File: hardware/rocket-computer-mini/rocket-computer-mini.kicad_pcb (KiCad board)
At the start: 6 copper layers, 222 parts, among them J2 TBLH11-350-05-BK, J3 JST_B2B-PH-SM4-TB, J6 USB4110GFA, J8 CON-SMA-EDGE-S, Q11 AONR21321, Q12 DTC123J, Q3 DTC123J, Q4 DTC123J, Q5 DTC123J, Q6 DTC123J, SW2 R-667995, SW3 R-667995, U1 FSUSB63UMX, U10 WSD20L50DN33, U11 GD5F1GQ5UEYIGR, U13 GD25Q128ESIG, U15 ESP32-S3RH2, U16 E220-900MM22S, U18 TPS62152RGTR, U19 TPS259631DDAR, U2 ISM6HG256XTR, U21 TPS2121RUXR, U23 INA230AIRGTR, U3 QMC5883P, U30 TPS22810DRVR, U31 ANT016008LCS2442MA2, U32 ESP32-S3RH2, U33 GD25Q128ESIG, U4 BMP581, U40 LM66100DCK, U41 74LVC1G17, U42 TPS22810DRVR, U44 LM66100DCK, U45 TPS3840PL29, U5 LC86GLAMD, U6 WSD20L50DN33, U7 WSD20L50DN33, U8 WSD20L50DN33, U9 AON7534, Y1 ABS07-32.768KHZ-T, Y2 ECS-400-10-37B2-CKY-TR, Y3 ABS07-32.768KHZ-T, Y4 ECS-400-10-37B2-CKY-TR

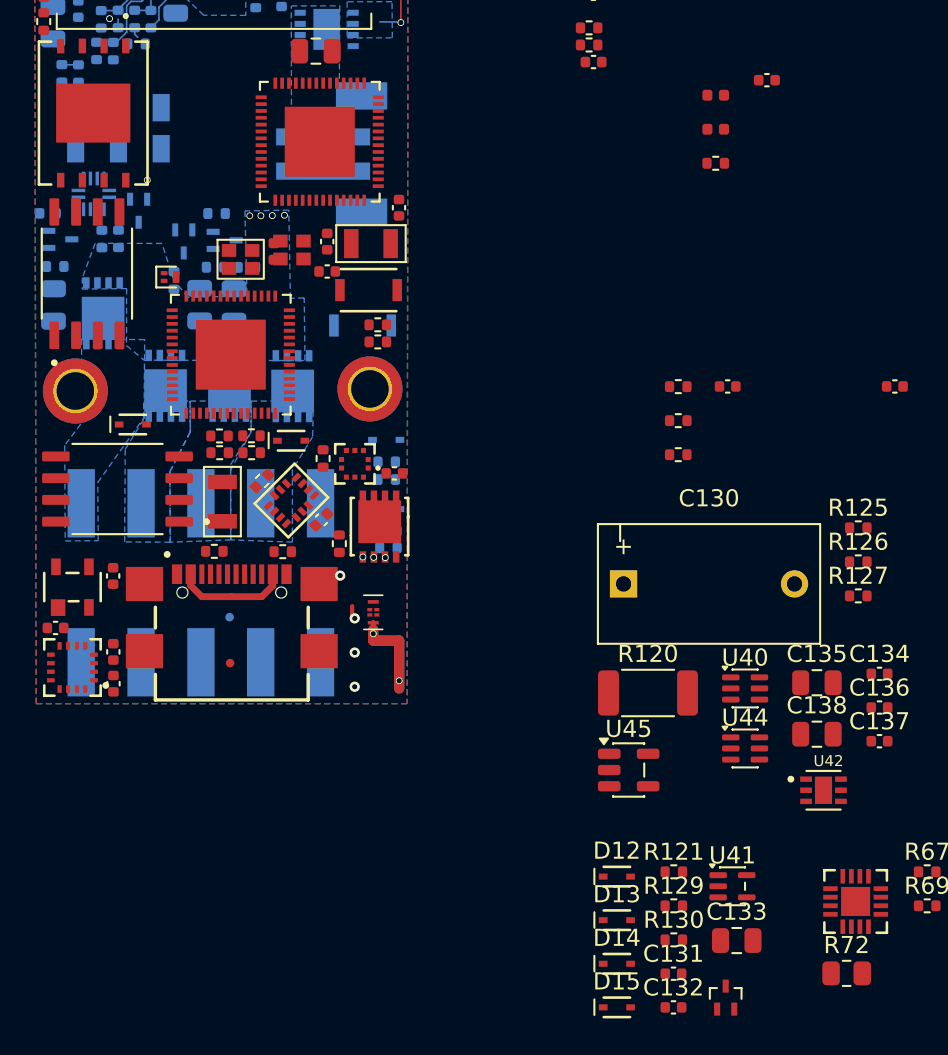
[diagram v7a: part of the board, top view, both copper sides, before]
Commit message: hardware: BOM re-use pass, DTC123J land fix, and pyro one-shot RC rework
Re-use pass across both rocket computers. The 17 new passives per board drawn
for the pack-fire/supercap rework carried no MPN field at all and would have
exported as blank BOM lines; assigning already-stocked parts rather than new
ones collapsed 15 would-be-new lines to zero.

Pyro arm one-shot (both boards):
- R131 added in parallel with R121 (2x 1M = 500k), C133/C138 moved to the
  stocked 22uF 0805, deleting the 10uF 0805 line.
- Not just BOM tidiness: SN74LVC1G17 Ii is +/-5uA max (SCES351Y Tbl 5-1). On
  the high-impedance timer node that offsets the asymptote to Vgate - Ii*R, so
  a single 1M settles near 1.0V, under VT+ max 1.92V, and a worst-case
  conforming part would NEVER trip the crowbar - the arm gate would stay up
  indefinitely. Max permissible R at the 2.83V supervisor floor is ~590k;
  500k clears it with ~19% headroom. Do not collapse R131 back into one 1M.
- R130 22k -> stocked 10k. With C133 now 22uF the reset stays at 0.22s, so the
  two edits cancel and the >=0.5s inter-arm spacing rule is unchanged.
- Ceiling ~3.4s nominal, 1.7s fast corner. The pyro sheet note now carries the
  leakage constraint so it cannot be "simplified" away later.

DTC123J land (affects Q3-Q6 on both boards, not only the rework):
- Widened to ROHM's own recommended pattern (Land Pattern Reference,
  Transistor, Rev.001 p.1/6): pair 0.6x0.7 on 1.0mm pitch, lone pad 0.7x0.7,
  rows 1.3 c-c. The inherited land was an imperial 14x30 mil pattern, 30-50%
  narrow across the lead with almost no side fillet on the widest terminal.
- Renamed DTC123JEBTL -> TRANS_SOT-416_EMT3-EMT3F_ROHM. ROHM publishes ONE
  land for both the gull-wing EMT3 and the flat-lead EMT3F, so naming it after
  either part number was misleading.
- rocket-computer-mini Q12 -> DTC123JETL, matching its Q3-Q6. MPN field only.

NOTE: the wider pads collide with existing routing on rocket-computer - two
genuine pad-to-via shorts (Q3 GND v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
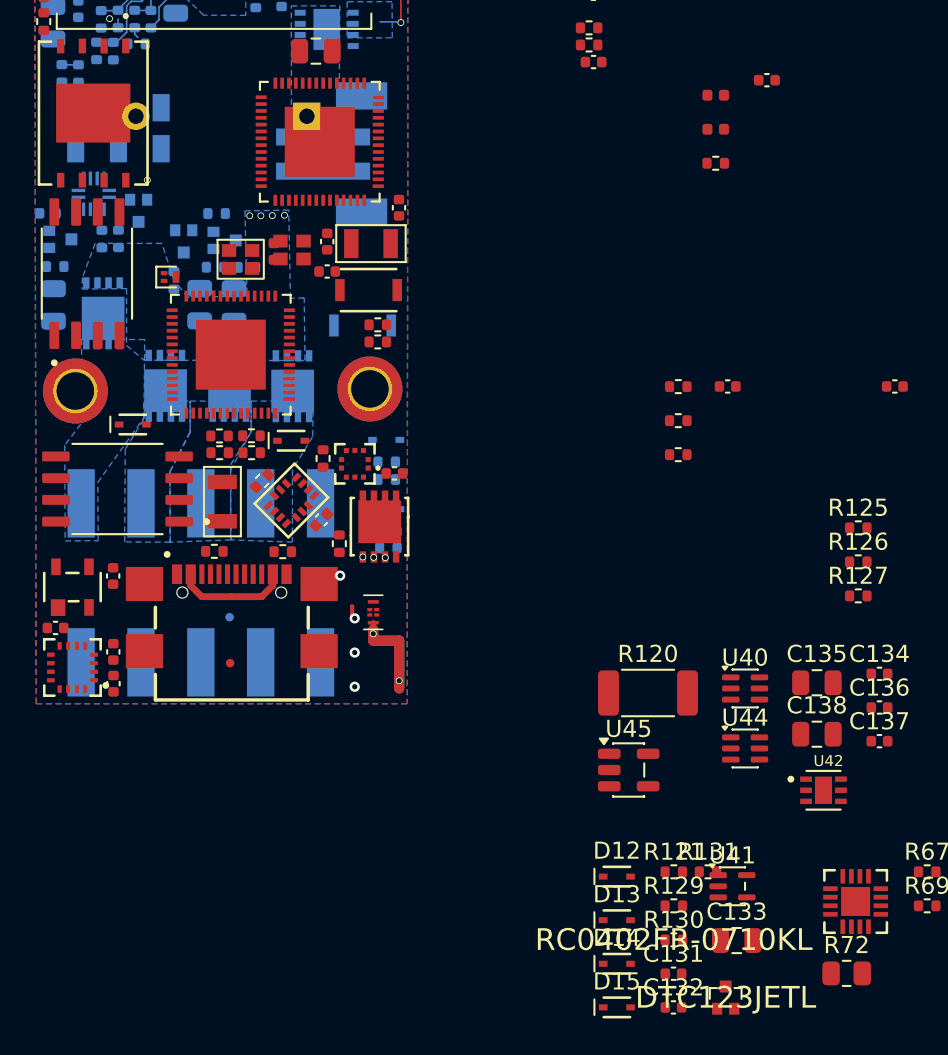
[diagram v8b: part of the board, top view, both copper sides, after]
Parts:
- added R131: 1 M, Resistor_SMD:R_0402_1005Metric, F.Cu at (112.2, 181.1)
- C130: footprint Footprints:Supercap_Prismatic_13.0x7.0mm_H28.5mm_P10.00mm -> Footprints:Supercap_Prismatic_13.0x7.0mm_L28.5mm_P10.00mm_Horizontal; moved to B.Cu
- Q12, Q3, Q4, Q5, Q6: footprint Footprints:DTC123JEBTL -> Footprints:TRANS_SOT-416_EMT3-EMT3F_ROHM
- R130: value 22 k -> 10 k
- moved C130 39.5 mm to (83.8, 136.9), turned to 90 degrees
